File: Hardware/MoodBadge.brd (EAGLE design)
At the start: 195.6 x 195.6 mm, 80 parts, among them IC1 PCF8574T, U1 MCP73831, U2 ATMEGA328P_TQFP

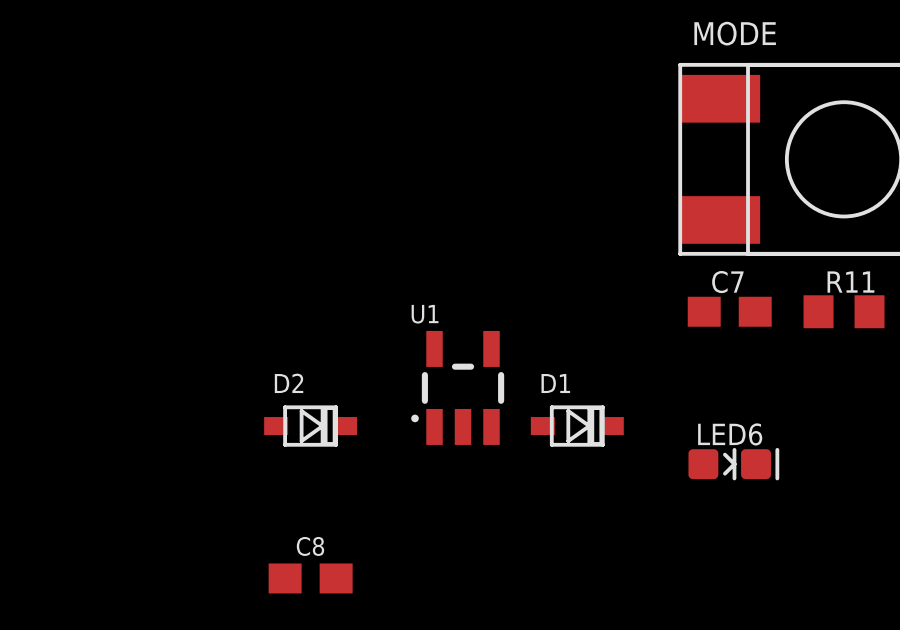
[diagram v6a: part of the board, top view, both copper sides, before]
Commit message: Fixed incorrect values and made organizational adjustments
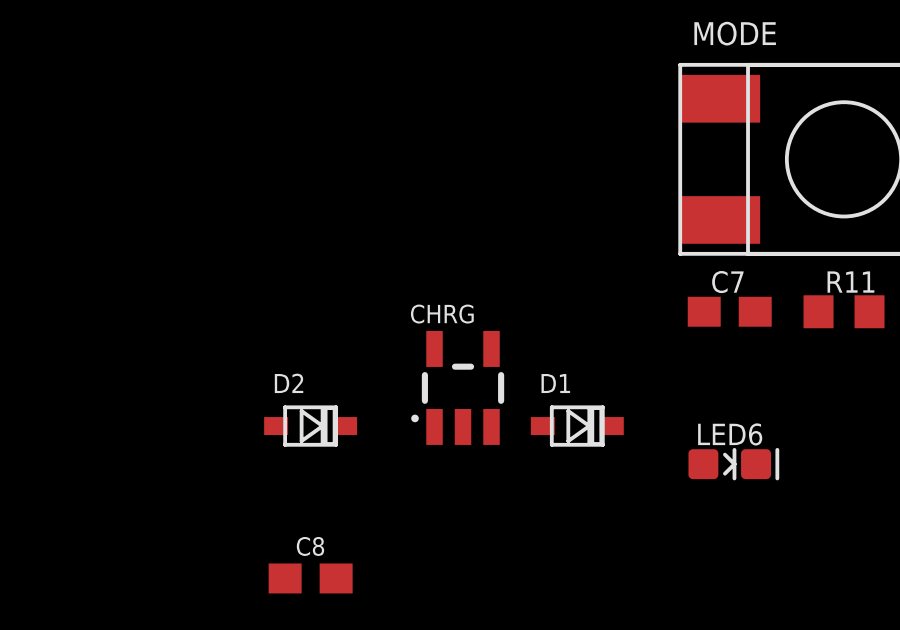
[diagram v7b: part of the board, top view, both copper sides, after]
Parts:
- LED1: value (none) -> LEFT
- LED2: value (none) -> SELECT
- LED3: value (none) -> DOWN
- LED4: value (none) -> UP
- LED5: value (none) -> RIGHT
- LED6: value (none) -> MODE
- LED7: value (none) -> STAT
- R14: value 1k -> 10K
- Y1: value (none) -> Crystal-CA-310
- renumbered U1 to CHRG
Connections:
- net LD4: now also U2.22
- net LD5: now also U2.19
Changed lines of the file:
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@@
 <attribute name="VALUE" x="-106.045" y="-217.805" size="0.7112" layer="27"/>
 </element>
-<element name="LED1" library="LinnesLab-LED" package="LED-0603" package3d_urn="urn:adsk.eagle:package:18593052/2" value="" x="-104.14" y="-238.76" smashed="yes">
+<element name="LED1" library="LinnesLab-LED" package="LED-0603" package3d_urn="urn:adsk.eagle:package:18593052/2" value="LEFT" x="-104.14" y="-238.76" smashed="yes">
 <attribute name="NAME" x="-104.14" y="-238.125" size="0.7112" layer="25" ratio="20" align="bottom-center"/>
 <attribute name="VALUE" x="-104.14" y="-239.395" size="0.7112" layer="27" ratio="20" align="top-center"/>
@@
 <attribute name="VALUE" x="-106.045" y="-252.095" size="0.7112" layer="27"/>
 </element>
-<element name="LED2" library="LinnesLab-LED" package="LED-0603" package3d_urn="urn:adsk.eagle:package:18593052/2" value="" x="-105.41" y="-255.27" smashed="yes">
+<element name="LED2" library="LinnesLab-LED" package="LED-0603" package3d_urn="urn:adsk.eagle:package:18593052/2" value="SELECT" x="-105.41" y="-255.27" smashed="yes">
 <attribute name="NAME" x="-105.41" y="-254.635" size="0.7112" layer="25" ratio="20" align="bottom-center"/>
 <attribute name="VALUE" x="-105.41" y="-255.905" size="0.7112" layer="27" ratio="20" align="top-center"/>
@@
 <attribute name="VALUE" x="-106.045" y="-268.605" size="0.7112" layer="27"/>
 </element>
-<element name="LED3" library="LinnesLab-LED" package="LED-0603" package3d_urn="urn:adsk.eagle:package:18593052/2" value="" x="-105.41" y="-271.78" smashed="yes">
+<element name="LED3" library="LinnesLab-LED" package="LED-0603" package3d_urn="urn:adsk.eagle:package:18593052/2" value="DOWN" x="-105.41" y="-271.78" smashed="yes">
 <attribute name="NAME" x="-105.41" y="-271.145" size="0.7112" layer="25" ratio="20" align="bottom-center"/>
 <attribute name="VALUE" x="-105.41" y="-272.415" size="0.7112" layer="27" ratio="20" align="top-center"/>
@@
 <attribute name="VALUE" x="-106.045" y="-285.115" size="0.7112" layer="27"/>
 </element>
-<element name="LED4" library="LinnesLab-LED" package="LED-0603" package3d_urn="urn:adsk.eagle:package:18593052/2" value="" x="-105.41" y="-288.29" smashed="yes">
+<element name="LED4" library="LinnesLab-LED" package="LED-0603" package3d_urn="urn:adsk.eagle:package:18593052/2" value="UP" x="-105.41" y="-288.29" smashed="yes">
 <attribute name="NAME" x="-105.41" y="-287.655" size="0.7112" layer="25" ratio="20" align="bottom-center"/>
 <attribute name="VALUE" x="-105.41" y="-288.925" size="0.7112" layer="27" ratio="20" align="top-center"/>
@@
 <attribute name="VALUE" x="-106.045" y="-301.625" size="0.7112" layer="27"/>
 </element>
-<element name="LED5" library="LinnesLab-LED" package="LED-0603" package3d_urn="urn:adsk.eagle:package:18593052/2" value="" x="-105.41" y="-304.8" smashed="yes">
+<element name="LED5" library="LinnesLab-LED" package="LED-0603" package3d_urn="urn:adsk.eagle:package:18593052/2" value="RIGHT" x="-105.41" y="-304.8" smashed="yes">
 <attribute name="NAME" x="-105.41" y="-304.165" size="0.7112" layer="25" ratio="20" align="bottom-center"/>
 <attribute name="VALUE" x="-105.41" y="-305.435" size="0.7112" layer="27" ratio="20" align="top-center"/>
@@
 <attribute name="VALUE" x="-106.045" y="-318.135" size="0.7112" layer="27"/>
 </element>
-<element name="LED6" library="LinnesLab-LED" package="LED-0603" package3d_urn="urn:adsk.eagle:package:18593052/2" value="" x="-105.41" y="-321.31" smashed="yes">
+<element name="LED6" library="LinnesLab-LED" package="LED-0603" package3d_urn="urn:adsk.eagle:package:18593052/2" value="MODE" x="-105.41" y="-321.31" smashed="yes">
 <attribute name="NAME" x="-105.41" y="-320.675" size="0.7112" layer="25" ratio="20" align="bottom-center"/>
 <attribute name="VALUE" x="-105.41" y="-321.945" size="0.7112" layer="27" ratio="20" align="top-center"/>
@@
 <attribute name="VALUE" x="-111.76" y="-321.705" size="0.635" layer="27"/>
 </element>
-<element name="U1" library="SparkFun-IC-Power" package="SOT23-5" value="MCP73831" x="-114.3" y="-318.77" smashed="yes">
+<element name="CHRG" library="SparkFun-IC-Power" package="SOT23-5" value="MCP73831" x="-114.3" y="-318.77" smashed="yes">
 <attribute name="NAME" x="-116.078" y="-316.611" size="0.6096" layer="25" ratio="20"/>
 <attribute name="PROD_ID" value="IC-09995" x="-114.3" y="-318.77" size="1.778" layer="27" display="off"/>
@@
 <attribute name="VALUE" x="-120.015" y="-330.835" size="0.7112" layer="27"/>
 </element>
-<element name="LED7" library="LinnesLab-LED" package="LED-0603" package3d_urn="urn:adsk.eagle:package:18593052/2" value="" x="-118.11" y="-334.01" smashed="yes">
+<element name="LED7" library="LinnesLab-LED" package="LED-0603" package3d_urn="urn:adsk.eagle:package:18593052/2" value="STAT" x="-118.11" y="-334.01" smashed="yes">
 <attribute name="NAME" x="-118.11" y="-333.375" size="0.7112" layer="25" ratio="20" align="bottom-center"/>
 <attribute name="VALUE" x="-118.11" y="-334.645" size="0.7112" layer="27" ratio="20" align="top-center"/>
 </element>
-<element name="R14" library="LinnesLab-Passives" package="R0603" package3d_urn="urn:adsk.eagle:package:15661944/2" value="1k" x="-119.38" y="-337.82" smashed="yes">
+<element name="R14" library="LinnesLab-Passives" package="R0603" package3d_urn="urn:adsk.eagle:package:15661944/2" value="10K" x="-119.38" y="-337.82" smashed="yes">
 <attribute name="NAME" x="-120.015" y="-337.185" size="0.7112" layer="25"/>
 <attribute name="VALUE" x="-120.015" y="-339.725" size="0.7112" layer="27"/>
@@
 <attribute name="VALUE" x="-130.175" y="-384.175" size="0.7112" layer="27"/>
 </element>
-<element name="Y1" library="LinnesLab-Clocks" package="CA-301" value="" x="-134.62" y="-382.27" smashed="yes">
+<element name="Y1" library="LinnesLab-Clocks" package="CA-301" value="Crystal-CA-310" x="-134.62" y="-382.27" smashed="yes">
 <attribute name="NAME" x="-135.89" y="-381" size="0.635" layer="25"/>
 <attribute name="VALUE" x="-135.89" y="-384.175" size="0.635" layer="22"/>
@@
 <contactref element="C8" pad="2"/>
 <contactref element="USB1" pad="5"/>
-<contactref element="U1" pad="2"/>
+<contactref element="CHRG" pad="2"/>
 <contactref element="C13" pad="2"/>
 <contactref element="C12" pad="2"/>
@@
 <contactref element="C1" pad="1"/>
 <contactref element="D1" pad="-"/>
-<contactref element="U1" pad="3"/>
+<contactref element="CHRG" pad="3"/>
 <contactref element="C9" pad="1"/>
 <wire x1="-101.6" y1="-100" x2="-106.26" y2="-113.03" width="0" layer="19" extent="1-1"/>
@@
 <contactref element="MODE" pad="2"/>
 <contactref element="D2" pad="-"/>
-<contactref element="U1" pad="4"/>
+<contactref element="CHRG" pad="4"/>
 <contactref element="C8" pad="1"/>
 <contactref element="R13" pad="2"/>
@@
 </signal>
 <signal name="N$4">
-<contactref element="U1" pad="5"/>
+<contactref element="CHRG" pad="5"/>
 <contactref element="R14" pad="2"/>
 <wire x1="-115.25" y1="-317.4699" x2="-118.53" y2="-337.82" width="0" layer="19" extent="1-1"/>
@@
 <signal name="STAT">
 <contactref element="LED7" pad="C"/>
-<contactref element="U1" pad="1"/>
+<contactref element="CHRG" pad="1"/>
 <wire x1="-115.25" y1="-320.0701" x2="-117.233" y2="-334.01" width="0" layer="19" extent="1-1"/>
 </signal>
@@
 <signal name="LD5">
 <contactref element="R23" pad="1"/>
+<contactref element="U2" pad="19"/>
+<wire x1="-182.46" y1="-436.88" x2="-122.7074" y2="-347.91" width="0" layer="19" extent="1-1"/>
 </signal>
 <signal name="LD4">
 <contactref element="MATRIX" pad="4"/>
+<contactref element="U2" pad="22"/>
+<wire x1="-165.1" y1="-391.73" x2="-122.7074" y2="-345.51" width="0" layer="19" extent="1-1"/>
 </signal>
 <signal name="RXD">

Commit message: Placed the matrix and the direction buttons
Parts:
- moved C16 476.3 mm to (-233.7, 2.54)
- moved C17 476.3 mm to (-233.7, -1.27)
- moved C18 476.3 mm to (-233.7, -5.08)
- moved C19 476.3 mm to (-233.7, -8.89)
- moved C20 476.3 mm to (-233.7, -36.8)
- moved C21 476.3 mm to (-233.7, -40.6)
- moved R18 476.3 mm to (-231.1, 62.2)
- moved R21 476.3 mm to (-231.1, 47.0)
- moved R22 476.3 mm to (-231.1, 41.9)
- moved R26 476.3 mm to (-234.9, -12.7)
- moved R27 476.3 mm to (-234.9, -21.6)
- moved C15 476.3 mm to (-231.1, 11.4)
- moved IC1 476.3 mm to (-224.8, 27.9)
- moved LED8 476.3 mm to (-229.9, 20.3)
- moved OP 476.3 mm to (-233.7, -44.5)
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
